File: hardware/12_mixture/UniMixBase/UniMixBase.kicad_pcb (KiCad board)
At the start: 4 copper layers, 122 x 171 mm, 145 parts, among them IC1 VNN3NV04PTR-E, IC11 VNN3NV04PTR-E, IC2 VNN3NV04PTR-E, IC3 VNN3NV04PTR-E, IC4 VNN3NV04PTR-E, IC5 VNN3NV04PTR-E, IC6 VNN3NV04PTR-E, IC7 VNN3NV04PTR-E, IC8 VNN3NV04PTR-E, J1 Conn_01x04_Male, J10 Conn_01x03_Pin, J11 Conn_01x02_Male, J12 Conn_01x02_Male, J13 Conn_01x02_Male, J14 Conn_01x04_Male, J18 Conn_01x04_Male, J2 Conn_01x04_Male, J20 Conn_01x04_Male, J21 Conn_01x04_Male, J22 Conn_01x03_Pin, J24 Conn_01x04_Male, J3 Conn_01x04_Male, J31 Conn_01x02_Male, J32 Conn_01x02_Male, J33 Conn_01x02_Male, J4 Conn_01x04_Male, J5 Conn_01x04_Male, J6 Conn_01x03_Pin, J7 Conn_01x04_Male, J8 Conn_01x04_Male, J9 Conn_01x04_Male, U1 NUCLEO-H755, U10 74AHC04, U11 MP1584 DC/DC, U12 TCA9802, U13 TMC2209_SILENTSTEPSTICK, U2 TMC2209_SILENTSTEPSTICK, U3 TMC2209_SILENTSTEPSTICK, U4 TMC2209_SILENTSTEPSTICK, U5 74AHC04, U6 TMC2209_SILENTSTEPSTICK, U7 TMC2209_SILENTSTEPSTICK, U8 MP1584 DC/DC, U9 74AHC04

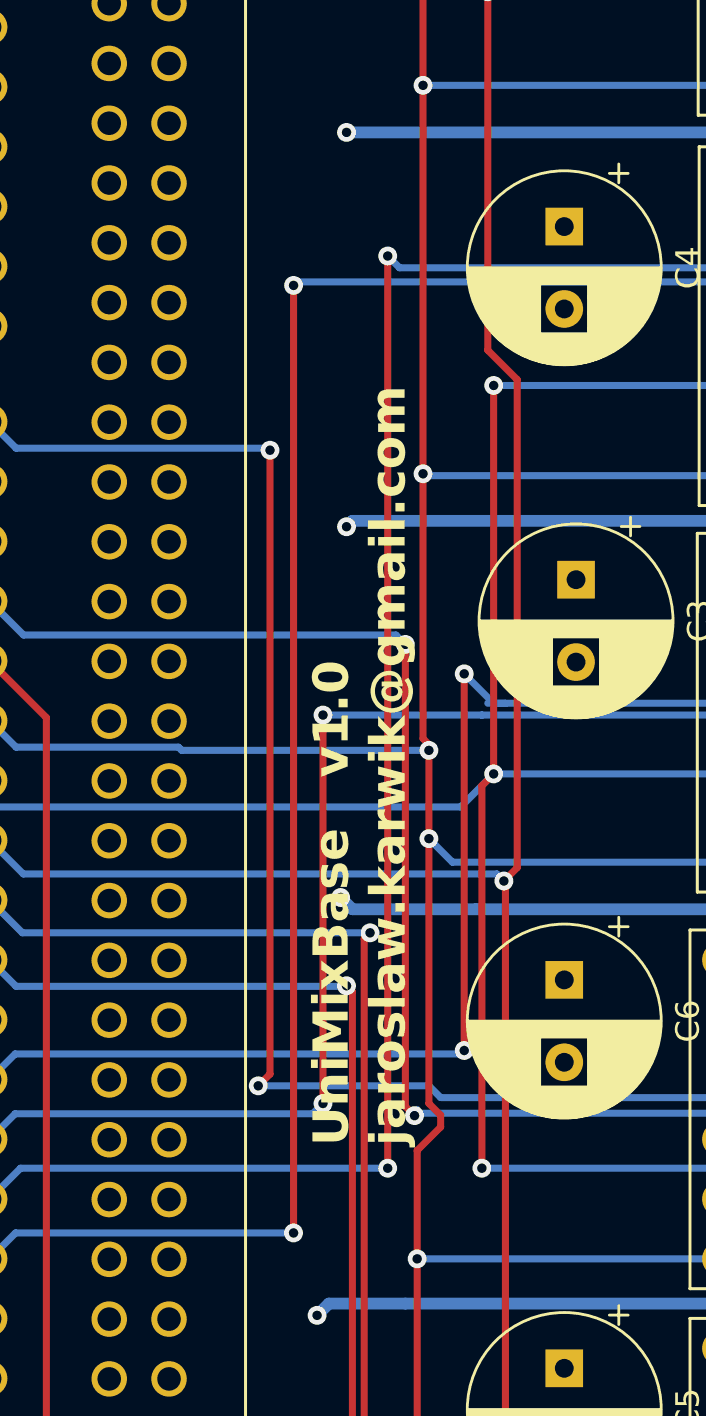
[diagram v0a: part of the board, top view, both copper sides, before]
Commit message: Github link added to PCB texts
Signed-off-by: Jaroslaw Karwik <jaroslaw.karwik@gmail.com>
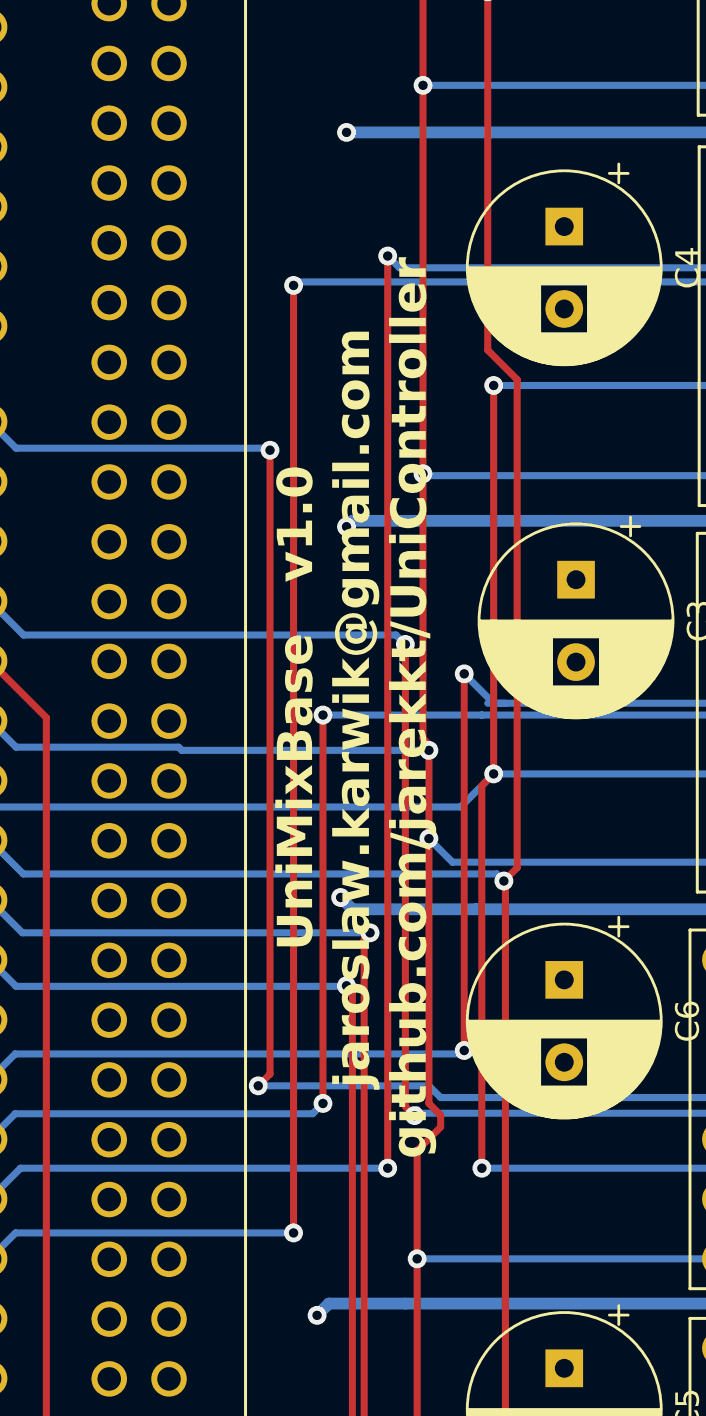
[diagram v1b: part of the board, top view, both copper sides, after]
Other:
- board text added: "UniMixBase v1.0 jaroslaw.karwik@gmail.com github.com/jarekkt/UniController"
- board text removed: "UniMixBase v1.0 jaroslaw.karwik@gmail.com"
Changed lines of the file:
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@@
 		)
 	)
-	(gr_text "UniMixBase   v1.0\njaroslaw.karwik@gmail.com"
-		(at 123.9 137.8 90)
+	(gr_text "UniMixBase   v1.0  \njaroslaw.karwik@gmail.com\ngithub.com/jarekkt/UniController"
+		(at 124.8 119.2 90)
 		(layer "F.SilkS")
 		(effects
@@
 				(bold yes)
 			)
-			(justify left bottom)
+			(justify bottom)
 		)
 	)

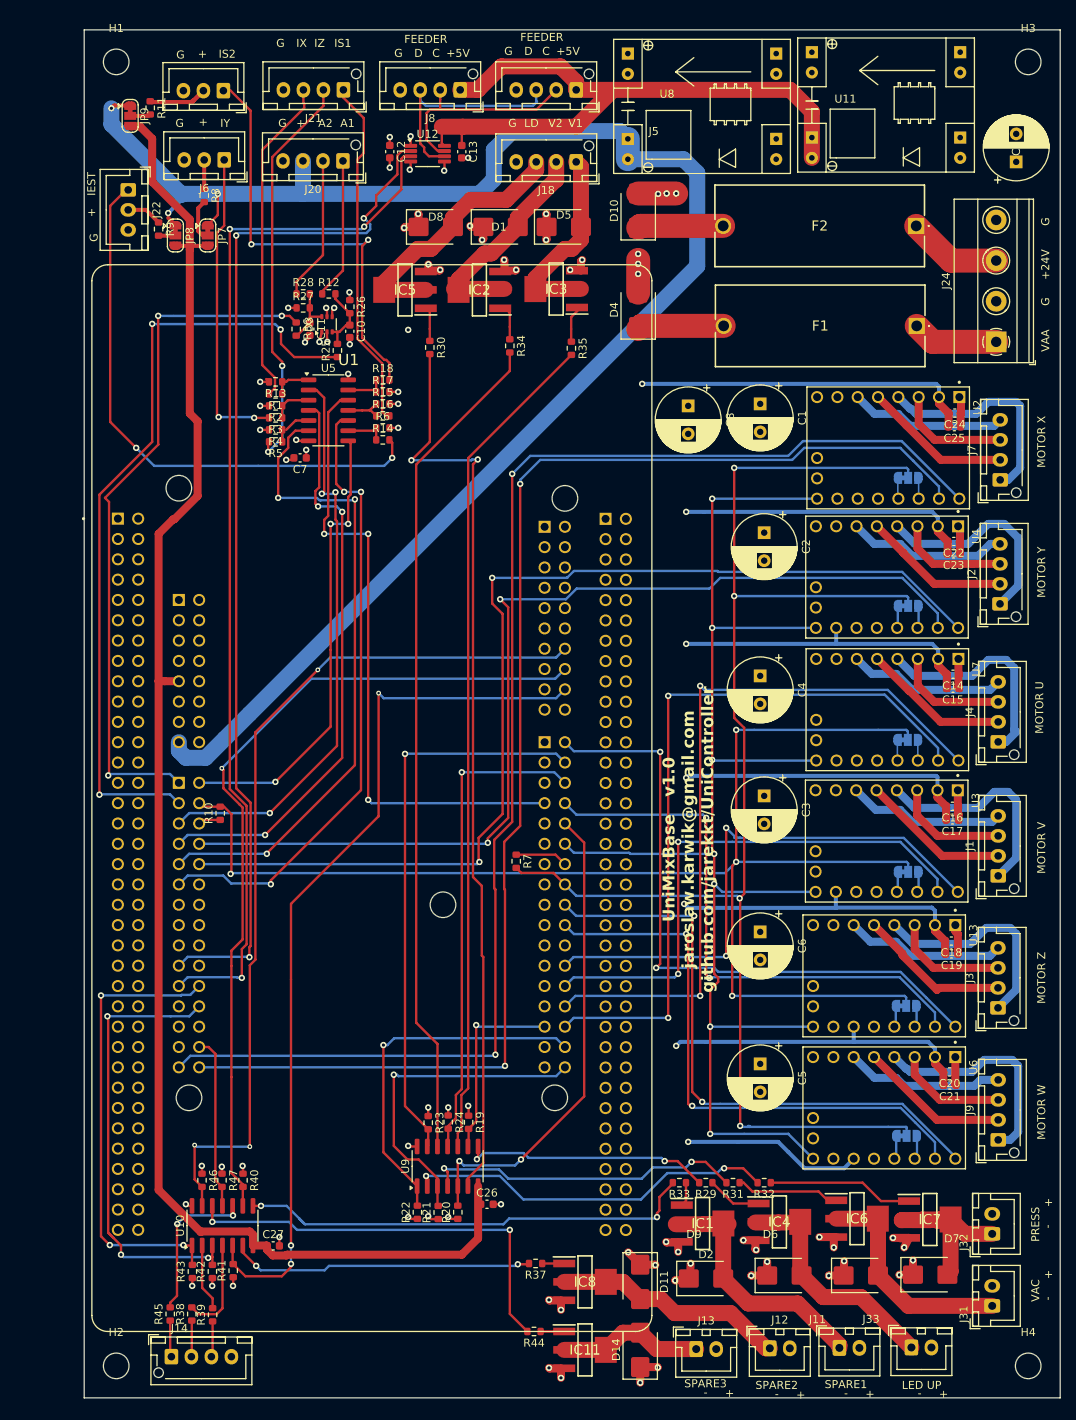
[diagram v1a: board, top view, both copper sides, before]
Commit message: Upadtes for Nucleo version
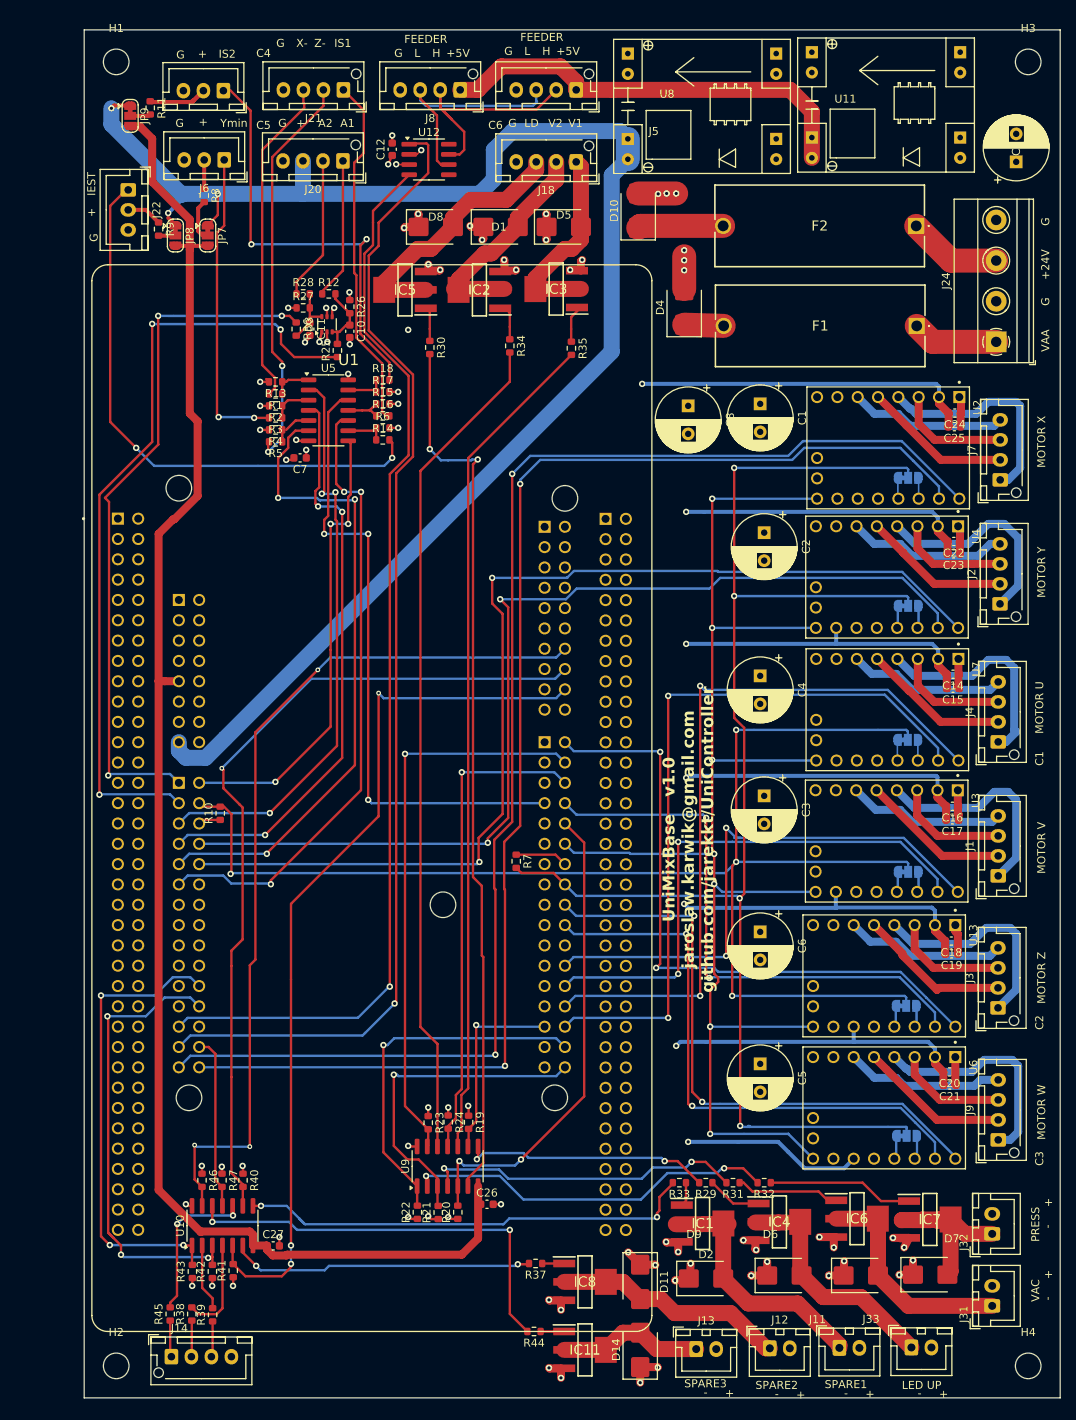
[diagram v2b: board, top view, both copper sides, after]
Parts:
- removed C13: 100n, Capacitor_SMD:C_0603_1608Metric
- U12: value TCA9802 -> SN65HVD232; footprint Package_SO:VSSOP-8_3x3mm_P0.65mm -> Package_SO:SOIC-8_3.9x4.9mm_P1.27mm
- moved D4 5.76 mm to (121.0, 52.7)
- moved U12 0.75 mm to (89.1, 34.2)
- moved C12 0.42 mm to (84.5, 32.9), turned to 90 degrees
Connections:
- net Net-(J5-Pin_2) renamed /CANH
- net Net-(J5-Pin_3) renamed /CANL
- U1 pad CN9_19: /SCL -> unconnected-(U1D-D69/I2C_B_SCL-PadCN9_19)
- U1 pad CN9_21: /SDA -> unconnected-(U1D-D68/I2C_B_SDA-PadCN9_21)
- U1 pad CN9_25: unconnected-(U1D-D67/CAN_RX-PadCN9_25) -> /CAN_RX
- U1 pad CN9_27: unconnected-(U1D-D66/CAN_TX-PadCN9_27) -> /CAN_TX
- U12 pad 1: +3.3V -> /CAN_TX
- U12 pad 2: /SCL -> GND
- U12 pad 3: /SDA -> +3.3V
- U12 pad 4: GND -> /CAN_RX
- U12 pad 5: +3.3V -> unconnected-(U12-NC-Pad5)
- U12 pad 8: /FEEDER_5V -> unconnected-(U12-NC-Pad8)
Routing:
- net /CAN_TX: track 0.00 -> 145.3 mm, vias 0 -> 1
- net /CAN_RX: track 0.00 -> 135.4 mm, vias 0 -> 1
- net /SDA: track 131.7 -> 0.00 mm, vias 3 -> 0
- net /SCL: track 130.7 -> 0.00 mm, vias 3 -> 0
- net /FEEDER_5V: track 82.1 -> 53.9 mm
- net +8V: track 207.3 -> 196.0 mm
- net VAA: track 10.9 -> 4.94 mm
- net /CANH: track 26.0 -> 30.3 mm
- net Net-(R30-Pad2): track 115.0 -> 110.9 mm
- net /OUT12_SPARE6: track 57.2 -> 58.1 mm
- net /OUT11_SPARE5: track 57.7 -> 58.6 mm
- net /CANL: track 28.6 -> 29.3 mm
- net +3.3V: track 279.7 -> 279.1 mm, vias 26 -> 25
- net GND: track 80.0 -> 80.4 mm, vias 46 -> 45
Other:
- board text added: "C1"
- board text added: "C2"
- board text added: "C3"
- board text added: "C4"
- board text added: "C5"
- board text added: "C6"
- board text added: "H"
- board text added: "L"
- board text added: "X-"
- board text added: "Ymin"
- board text added: "Z-"
- board text removed: "C"
- board text removed: "D"
- board text removed: "IX"
- board text removed: "IY"
- board text removed: "IZ"

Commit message: Updated hardware design
Signed-off-by: Jaroslaw Karwik <jaroslaw.karwik@gmail.com>
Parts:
- added C13: 1uF, Capacitor_SMD:C_0603_1608Metric, F.Cu at (62.8, 50.8)
- added C28: 10uF, Capacitor_SMD:C_1206_3216Metric, F.Cu at (59.5, 53.5)
- added C29: 100n, Capacitor_SMD:C_0603_1608Metric, F.Cu at (48.8, 61.5)
- added C30: 100n, Capacitor_SMD:C_0603_1608Metric, F.Cu at (60.2, 55.8)
- added C31: 100n / 16V, Capacitor_SMD:C_0603_1608Metric, F.Cu at (78.5, 47.0)
- added C32: 100n, Capacitor_SMD:C_0603_1608Metric, F.Cu at (84.0, 39.2)
- added IC9: AP7375-50W5-7, footprints:SOT95P285X140-5N, F.Cu at (59.5, 50.2)
- added J15: Conn_01x06_Male, Connector_JST:JST_XH_B6B-XH-AM_1x06_P2.50mm_Vertical, F.Cu at (41.8, 63.8)
- added J16: Conn_01x06_Male, Connector_JST:JST_XH_B6B-XH-AM_1x06_P2.50mm_Vertical, F.Cu at (41.8, 44.0)
- added R48: 120R, Resistor_SMD:R_1206_3216Metric, F.Cu at (46.8, 67.5)
- added R49: 120R, Resistor_SMD:R_1206_3216Metric, F.Cu at (46.8, 73.0)
- added R50: 120R, Resistor_SMD:R_1206_3216Metric, F.Cu at (46.5, 47.8)
- added R51: 120R, Resistor_SMD:R_1206_3216Metric, F.Cu at (46.8, 53.0)
- added U14: AM26LV32xD, Package_SO:SOIC-16_3.9x9.9mm_P1.27mm, F.Cu at (54.8, 63.5)
- added U15: TLE9251VSJ, Package_SO:SOIC-8_3.9x4.9mm_P1.27mm, F.Cu at (80.0, 42.0)
- moved J14 20.7 mm to (42.0, 169.5), turned to -90 degrees
- moved J22 13.3 mm to (41.8, 29.0)
- moved R39 12.1 mm to (50.0, 177.8), turned to 0 degrees
- moved R38 9.92 mm to (50.0, 175.5), turned to 0 degrees
- moved R45 8.56 mm to (50.0, 173.2), turned to 0 degrees
- moved H2 8.50 mm to (41.5, 185.0)
- moved H1 8.02 mm to (42.0, 21.5)
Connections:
- U1 pad CN10_13: unconnected-(U1F-D26/QSPI_CS-PadCN10_13) -> /OUT2_VALVE1
- U1 pad CN10_19: unconnected-(U1F-D28/QSPI_BK1_IO3-PadCN10_19) -> /ENC2_CH1
- U1 pad CN10_21: unconnected-(U1F-D29/QSPI_BK1_IO1-PadCN10_21) -> /ENC2_CH2
- U1 pad CN10_31: unconnected-(U1F-D33/TIMER_D_PWM1-PadCN10_31) -> /IN6_SPARE2
- U1 pad CN10_4: /OUT2_VALVE1 -> unconnected-(U1F-D6/TIMER_A_PWM1-PadCN10_4)
- U1 pad CN10_7: /IN6_SPARE2 -> unconnected-(U1F-A6/ADC_A_IN-PadCN10_7)
- U1 pad CN7_1: unconnected-(U1E-D16/I2S_A_MCK-PadCN7_1) -> /ENC1_CH1
- U1 pad CN7_11: unconnected-(U1E-D21/I2S_B_MCK-PadCN7_11) -> /ENC1_CH2
- U1 pad CN7_12: unconnected-(U1E-D12/SPI_A_MISO-PadCN7_12) -> /OUT9_SPARE3
- U1 pad CN7_14: /OUT9_SPARE3 -> unconnected-(U1E-D11/SPI_A_MOSI/TIM_E_PWM1-PadCN7_14)
- U1 pad CN9_11: /IN5_SPARE1 -> unconnected-(U1D-A5/ADC3_INP6/I2C1_SCL-PadCN9_11)
- U1 pad CN9_13: unconnected-(U1D-D72/COMP1_INP-PadCN9_13) -> /DIR_X
- U1 pad CN9_14: unconnected-(U1D-D56/SAI_A_MCLK-PadCN9_14) -> /IN5_SPARE1
- U1 pad CN9_15: unconnected-(U1D-D71/COMP2_INP-PadCN9_15) -> /STEP_X
- U1 pad CN9_29: /DIR_X -> unconnected-(U1D-D65/IO-PadCN9_29)
- U1 pad CN9_30: /STEP_X -> unconnected-(U1D-D64/IO-PadCN9_30)
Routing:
- net /ENC2_CH2: track 0.00 -> 121.2 mm, vias 0 -> 3
- net /ENC2_CH1: track 0.00 -> 117.3 mm, vias 0 -> 3
- net /ENC1_CH2: track 0.00 -> 67.8 mm, vias 0 -> 3
- net /ENC1_CH1: track 0.00 -> 63.1 mm, vias 0 -> 3
- net +5VA: track 0.00 -> 44.7 mm, vias 0 -> 1
- net /IN6_SPARE2: track 79.5 -> 114.6 mm
- net Net-(J16-Pin_2): track 0.00 -> 31.0 mm
- net +5V: track 198.2 -> 226.7 mm, vias 0 -> 2
- net /CANH: track 30.3 -> 56.3 mm
- net Net-(J16-Pin_3): track 0.00 -> 23.1 mm
- net /DIR_X: track 174.4 -> 153.1 mm
- net /CANL: track 29.3 -> 50.6 mm
- net Net-(J15-Pin_5): track 0.00 -> 20.6 mm
- net +8V: track 196.0 -> 216.5 mm, vias 3 -> 5
- net Net-(J15-Pin_4): track 0.00 -> 18.1 mm
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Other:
- board size 122 x 171 mm -> 130.5 x 171 mm
- board text added: "ENC X"
- board text added: "ENC Y"
- board text added: "OS4"
- board text added: "OS5"
- board text added: "OS6"

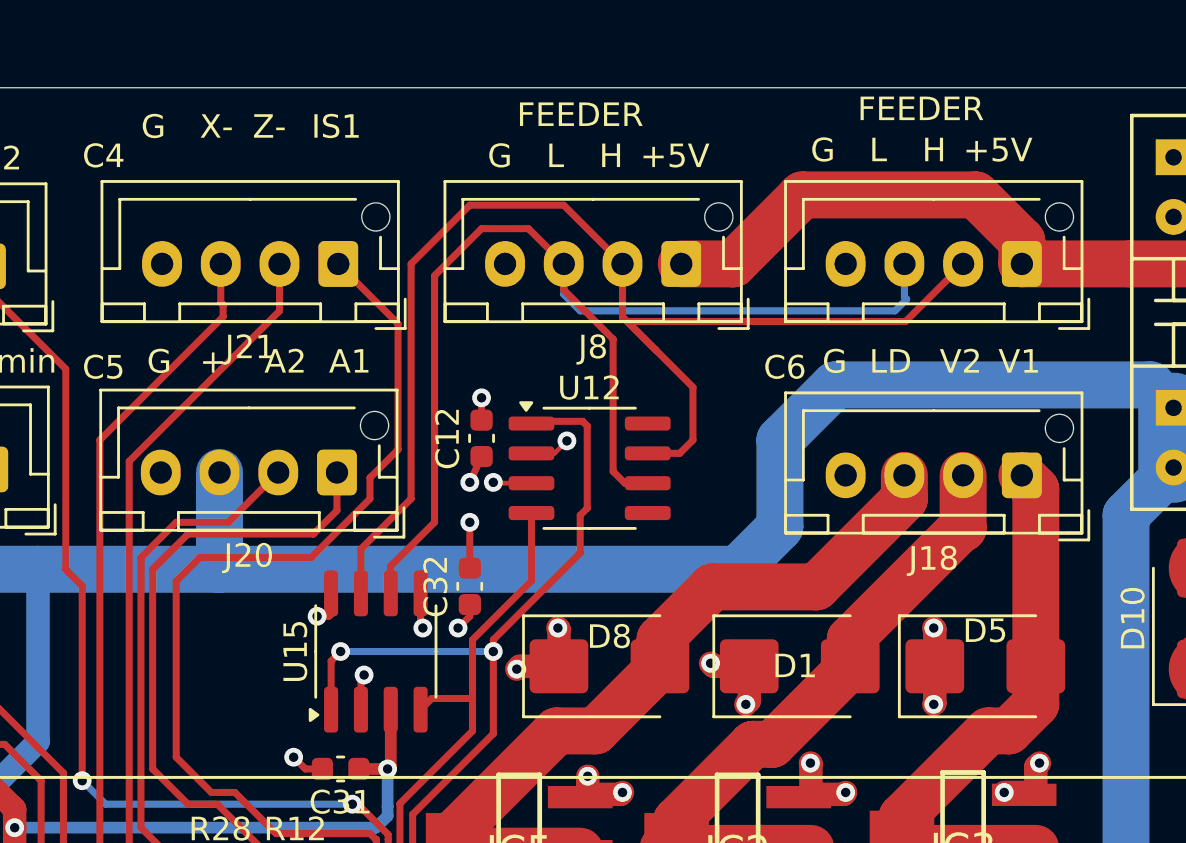
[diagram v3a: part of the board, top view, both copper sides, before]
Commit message: CAN FD head added
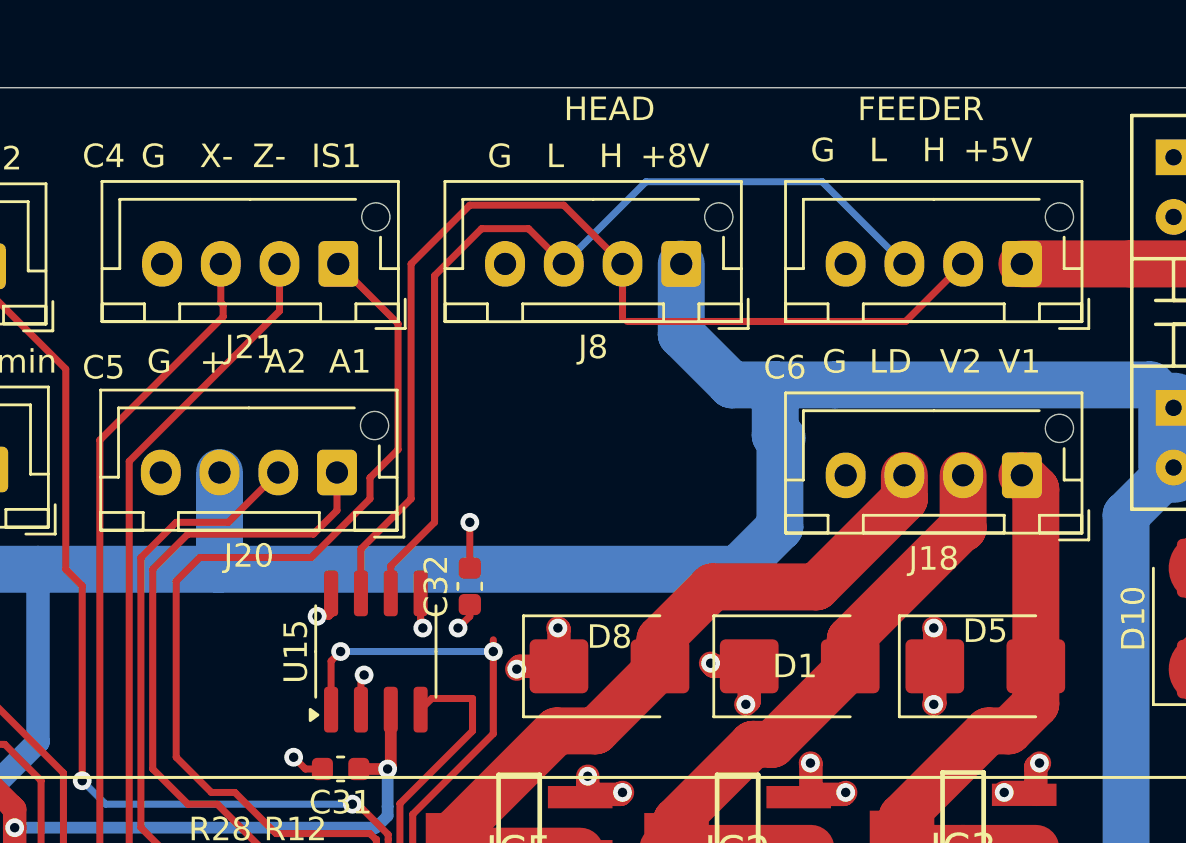
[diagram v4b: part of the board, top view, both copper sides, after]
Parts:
- removed C12: 100n, Capacitor_SMD:C_0603_1608Metric
- removed U12: SN65HVD232, Package_SO:SOIC-8_3.9x4.9mm_P1.27mm
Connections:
- J8 pad 1: /FEEDER_5V -> +8V
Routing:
- net /FEEDER_5V: track 53.9 -> 36.4 mm
- net /CAN_TX: track 154.5 -> 141.2 mm
- net /CANL: track 50.6 -> 38.6 mm
- net /CANH: track 56.3 -> 45.9 mm
- net +8V: track 216.5 -> 226.2 mm
- net /CAN_RX: track 137.8 -> 128.8 mm
- net +3.3V: track 291.1 -> 288.3 mm, vias 29 -> 27
- net GND: track 91.0 -> 88.3 mm, vias 52 -> 50
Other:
- board text added: "+8V"
- board text added: "HEAD"
